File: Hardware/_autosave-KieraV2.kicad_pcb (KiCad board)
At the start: 2 copper layers, 111 x 63.2 mm, 110 parts, among them J1 Conn_01x04_Male, J2 Conn_01x06_Male, SW1 SW_Rotary2x4, SW10 SW_Push, SW11 SW_Push, SW2 SW_Rotary2x4, SW3 SW_Push, SW4 SW_Push, SW5 SW_Push, SW6 SW_Push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

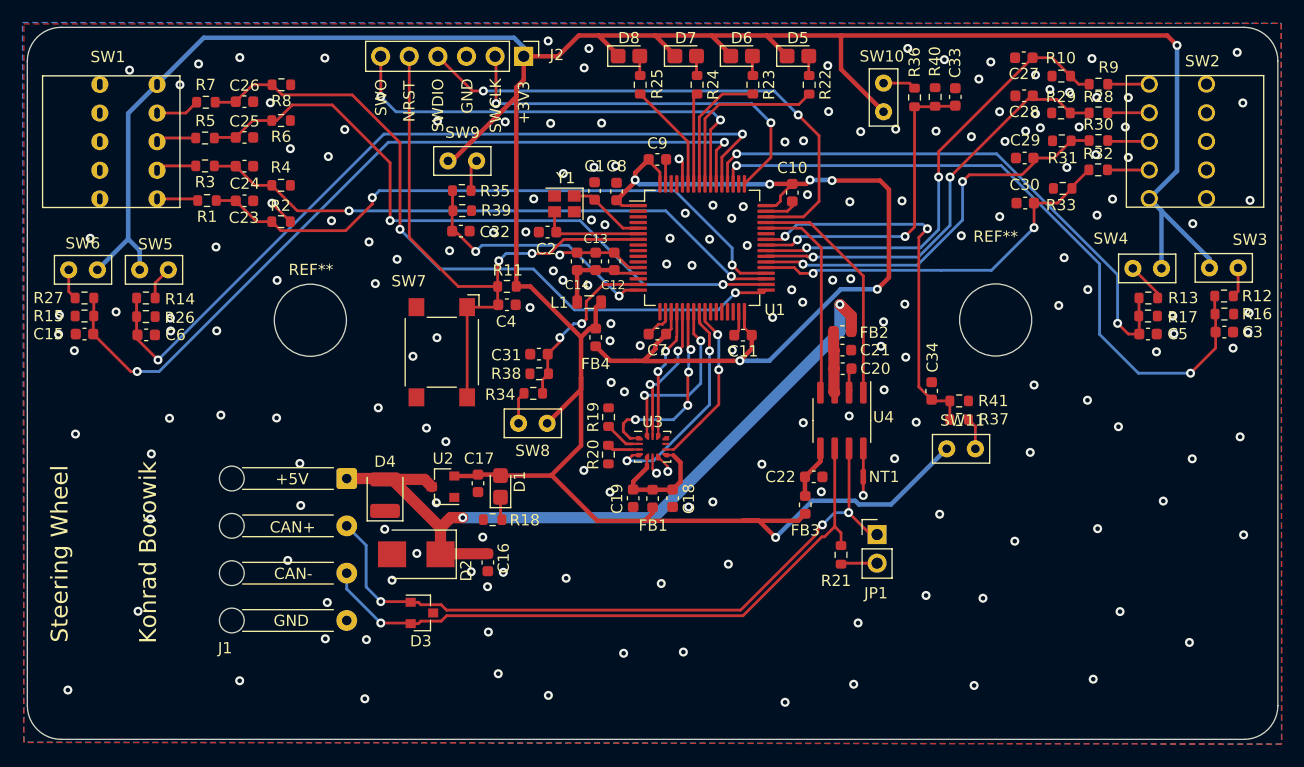
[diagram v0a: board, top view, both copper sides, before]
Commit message: changed positions for buttons
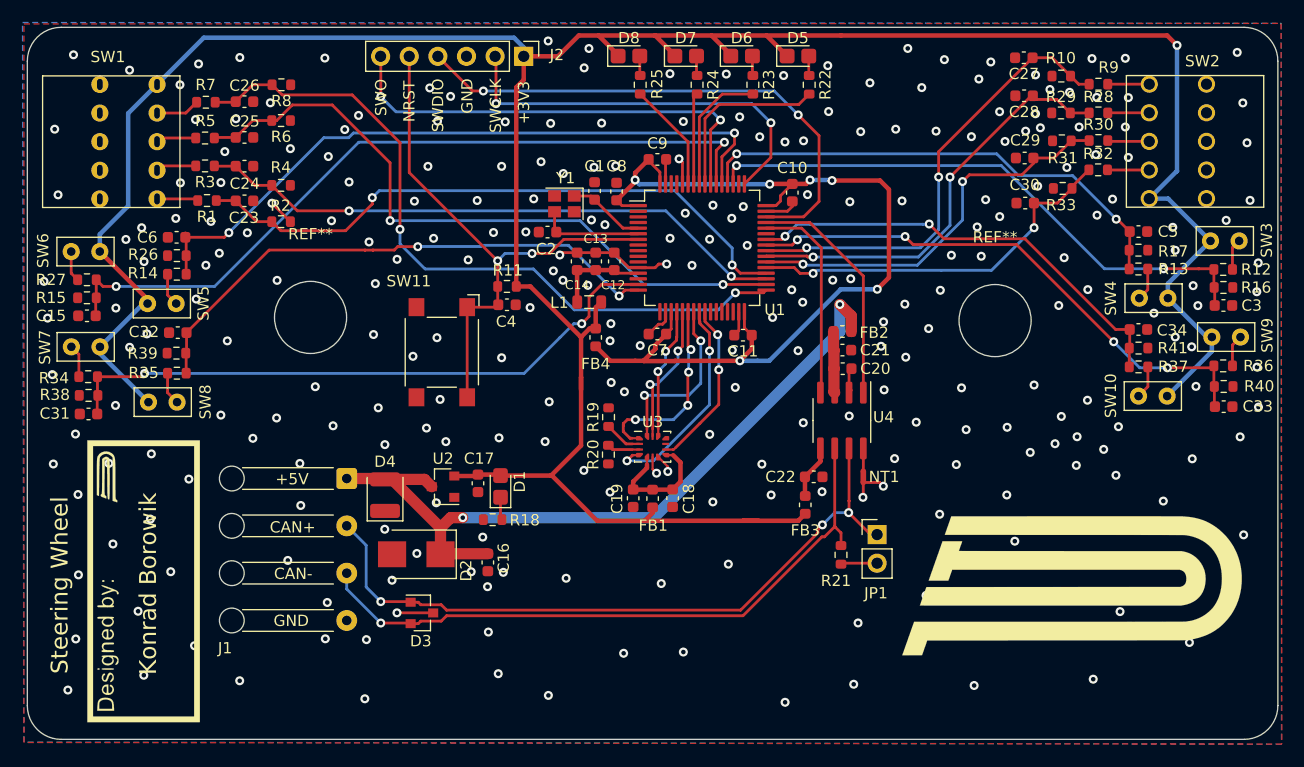
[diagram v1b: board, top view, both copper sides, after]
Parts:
- removed the REF** at (127.6, 115.8)
- removed the REF** at (188.4, 115.8)
- removed the SW9 at (141.1, 101.7)
- added G***: LOGO, Logos:SignatureBox25mm, F.Cu at (112.8, 139.0)
- added G***: LOGO, Logos:PUTM_LOGO_35mm, F.Cu at (194.3, 139.0)
- added REF**: MountingHole_6.4mm_M6, MountingHole:MountingHole_6.4mm_M6, F.Cu at (188.4, 115.8)
- added REF**: MountingHole_6.4mm_M6, MountingHole:MountingHole_6.4mm_M6, F.Cu at (127.6, 115.5)
- added SW7: SW_Push, Button_Switch_THT:MyPushbuttonSwitch, F.Cu at (107.7, 118.2)
- moved C31 40.3 mm to (107.9, 124.1)
- moved R38 40.0 mm to (107.9, 122.5)
- moved R34 39.5 mm to (107.9, 120.8)
- moved SW9 37.1 mm to (208.9, 117.3), turned to 0 degrees
- moved C33 36.4 mm to (208.7, 123.5), turned to 0 degrees
- moved R36 36.3 mm to (208.6, 119.8), turned to 0 degrees
- moved R40 36.3 mm to (208.7, 121.7), turned to 180 degrees
- moved SW8 32.9 mm to (114.5, 123.1), turned to 0 degrees
- moved R35 30.0 mm to (115.8, 120.5), turned to 180 degrees
- moved R39 28.3 mm to (115.7, 118.7), turned to 0 degrees
- moved C32 26.7 mm to (115.9, 116.9), turned to 180 degrees
- moved C34 19.1 mm to (201.1, 116.6), turned to 0 degrees
- moved SW10 17.7 mm to (202.4, 122.5), turned to 180 degrees
- moved R41 16.6 mm to (201.1, 118.3)
- moved R37 16.6 mm to (201.1, 119.9)
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- renumbered SW11 to SW10, SW7 to SW11, SW10 to SW9
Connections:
- SW8 pad 2: Net-(R34-Pad2) -> Net-(R35-Pad2)
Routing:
- net /SW7: track 15.5 -> 55.7 mm
- net /SW8: track 23.2 -> 48.9 mm
- net /SW9: track 28.2 -> 48.6 mm, vias 2 -> 4
- net +3V3: track 280.3 -> 265.2 mm, vias 2 -> 1
- net /SW5: track 71.6 -> 61.3 mm
- net /SW3: track 61.1 -> 51.2 mm
- net GND: track 29.4 -> 37.4 mm, vias 178 -> 261
- net /SW4: track 51.1 -> 44.2 mm
- net /SW10: track 34.5 -> 40.2 mm
- net /SW6: track 73.1 -> 68.6 mm
- net /NRST: track 53.7 -> 49.4 mm
- net /SW1_1: track 63.0 -> 63.8 mm
- net Net-(R13-Pad2): track 3.53 -> 2.90 mm
